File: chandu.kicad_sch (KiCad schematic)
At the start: 37 parts, among them IC1 bp060674p12, IC2 bp060674p12, J1 B5B-XH-A, J3 B5B-XH-A, J4 B2B-XH-A__LF__SN_, J5 B2B-XH-A__LF__SN_, J6 B4B-XH-A_LF__SN_, J7 51494-2, J8 51494-2, U1 KY-040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

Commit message: Initialtes
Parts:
- removed R_dac2_pup_scl1, R_dac2_pup_sda1, R_oled_pup_scl1, R_oled_pup_sda1: 4.7k, Resistor_THT:R_Axial_DIN0207_L6.3mm_D2.5mm_P7.62mm_Horizontal, symbol Device:R
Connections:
- net 3.3V: now also R_dac1_pup_scl1.2; no longer R_dac1_pup_scl1.1
- net at J6.2, U2.33 (IO21), U6.5 (SCL)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: now also R_dac1_pup_scl1.1; no longer R_dac1_pup_scl1.2
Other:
- moved on the sheet: D2, R_dac1_pup_scl1, R_dac1_pup_sda1

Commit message: Initialtes
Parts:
- U2: footprint kaam25_footprints_symbol:MODULE_DEVKIT_V1_ESP32-WROOM-32 -> kaam25:MODULE_DEVKIT_V1_ESP32-WROOM-32; Distributer https://robu.in/product/esp-wroom-32-wifi-bluetooth-network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 -> (none)
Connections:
- net 3.3V: no longer U2.1 (3V3)
- net GND2: now also U2.13 (IO12); no longer U2.14 (GND1)
- net at J6.3, R_dac1_pup_sda1.2, U6.4 (SDA)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: now also U2.37 (IO23); no longer U2.36 (IO22)
- net at J6.2, R_dac1_pup_scl1.1, U6.5 (SCL)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: now also U2.34 (RXD0); no longer U2.33 (IO21)
- net at R1.2, R3.1: now also U2.5 (IO34); no longer U2.6 (IO35)
- net at J5.1: now also U2.38 (GND3); no longer U2.37 (IO23)
- net at R5.2, R7.1: now also U2.7 (IO32); no longer U2.8 (IO33)
- net at R6.2, R8.1: now also U2.3 (SENSOR_VP); no longer U2.4 (SENSOR_VN)
- net at R2.2, R4.1: now also U2.2 (EN); no longer U2.3 (SENSOR_VP)
- net at U2.10 (IO26): now also J1.1; no longer J3.3
- net at U2.11 (IO27): no longer J1.1
- net at J3.5: now also U2.14 (GND1); no longer U2.15 (IO13)
- net at U2.26 (IO4): no longer J4.2
- net at U2.27 (IO16): now also J4.2
- net at U2.31 (IO19): no longer J3.4
- net at U2.32 (GND2): now also J3.4
- net at J1.3: now also U2.4 (SENSOR_VN); no longer U2.5 (IO34)
- net at J1.2: now also U2.6 (IO35); no longer U2.7 (IO32)
- net at U2.9 (IO25): now also J3.3
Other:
- moved on the sheet: J4

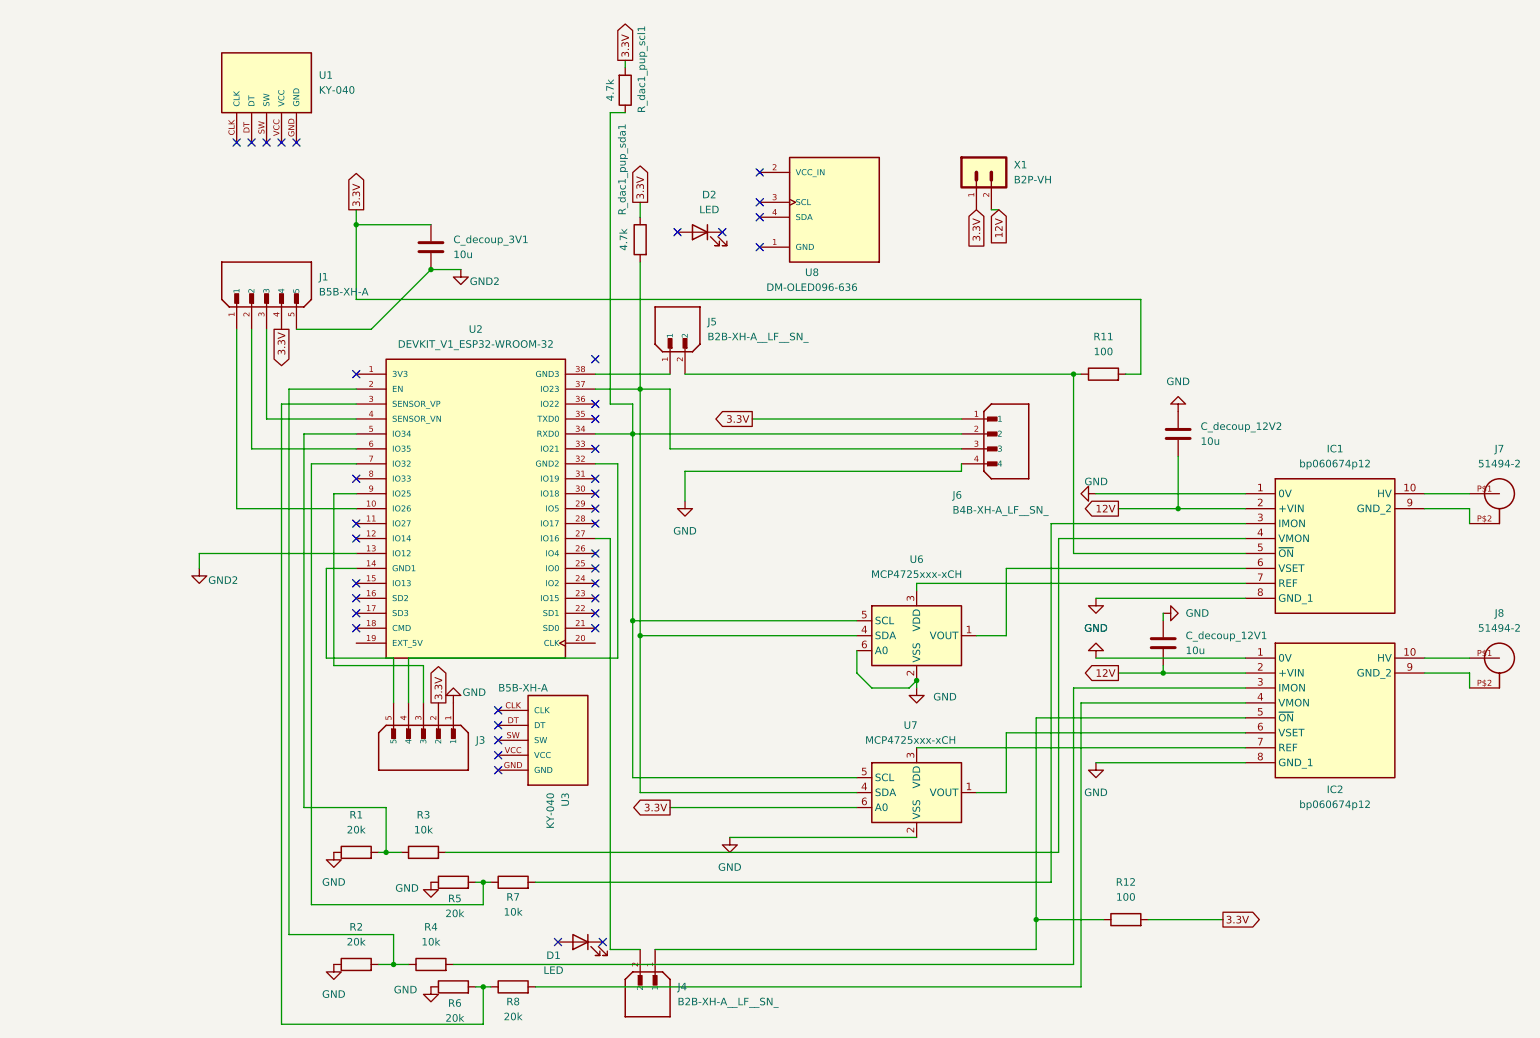
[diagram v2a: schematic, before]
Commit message: Initialtes gndplane
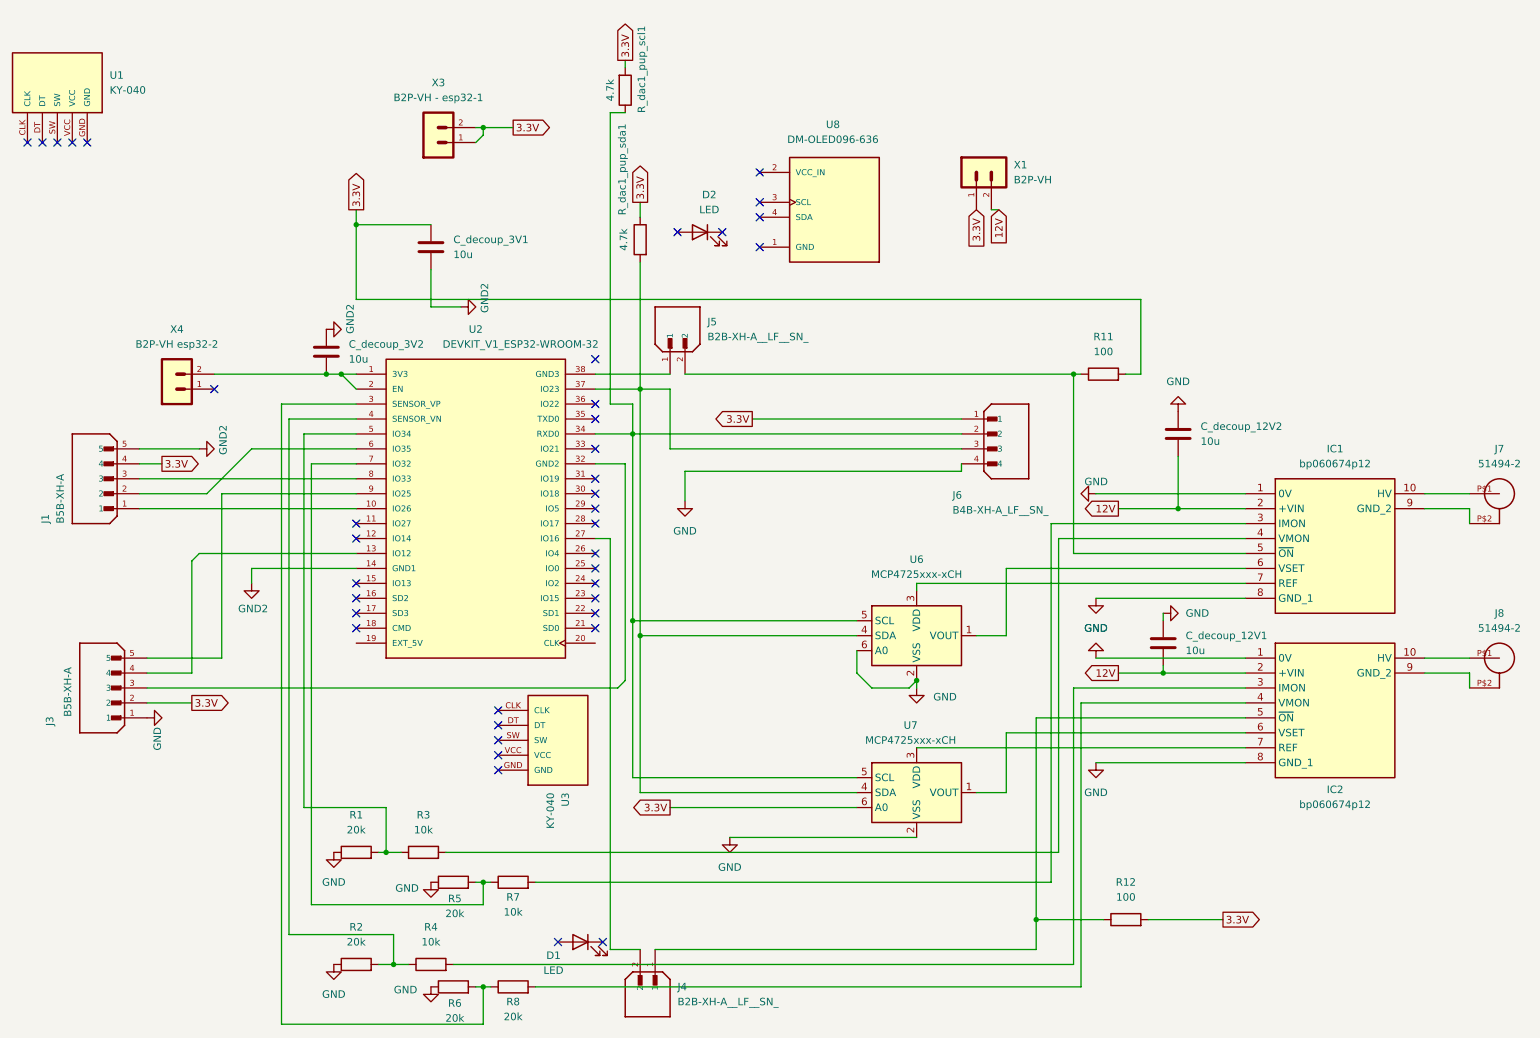
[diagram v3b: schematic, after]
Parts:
- added C_decoup_3V2: 10u, Capacitor_THT:CP_Radial_D5.0mm_P2.00mm, symbol Device:C
- added X3: B2P-VH - esp32-1, symbol B2P-VH:B2P-VH
- added X4: B2P-VH esp32-2, symbol B2P-VH:B2P-VH
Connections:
- net 3.3V: now also X3.1, X3.2
- net GND2: now also U2.14 (GND1), C_decoup_3V2.1; no longer U2.13 (IO12)
- net at R2.2, R4.1: now also U2.4 (SENSOR_VN); no longer U2.2 (EN)
- net at U2.1 (3V3): now also U2.2 (EN), C_decoup_3V2.2, X4.2
- net at J3.5: now also U2.9 (IO25); no longer U2.14 (GND1)
- net at J3.4: now also U2.13 (IO12); no longer U2.32 (GND2)
- net at J1.3: now also U2.8 (IO33); no longer U2.4 (SENSOR_VN)
- net at J3.3: now also U2.32 (GND2); no longer U2.9 (IO25)
- no-connect marks 40 -> 39
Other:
- moved on the sheet: J1, J3, U1

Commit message: Initialtes apr22
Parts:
- removed X3: B2P-VH - esp32-1, symbol B2P-VH:B2P-VH
- removed X4: B2P-VH esp32-2, symbol B2P-VH:B2P-VH
- added J10, J9: B2B-XH-A, kaam25:B2P-VH, symbol B2B-XH-A:B2B-XH-A
- J1, J3: value B5B-XH-A -> B5B-XH-A_rotataryKnob
- J4, J5: value B2B-XH-A__LF__SN_ -> B2B-XH-A__LF__SN_ledTwoTerminal
- J6: value B4B-XH-A_LF__SN_ -> B4B-XH-A_LF__SN_oled_display
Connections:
- net 3.3V: now also J10.1, J10.2
- net at C_decoup_3V2.2, U2.1 (3V3), U2.2 (EN): now also J9.2

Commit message: Initialtes apr24
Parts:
- added X3: B2P-VH, Connector_JST:JST_VH_B2P-VH-B_1x02_P3.96mm_Vertical, symbol B2P-VH:B2P-VH
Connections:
- net GND2 is gone; now on net GND1: C_decoup_3V1.2, C_decoup_3V2.1, J1.5, U2.14 (GND1)
- net 12V: now also X3.2
- net 3.3V: now also X3.1; no longer J1.4
- net vset_a: now reaches IC1.6 (VSET), U6.1 (VOUT)
- net ref_b: now reaches IC1.7 (REF), U6.3 (VDD)
- net ref_b: now also IC2.7 (REF), U7.3 (VDD)
- net sda_a: now reaches J6.3, R_dac1_pup_sda1.2, U2.37 (IO23), U6.4 (SDA), U7.4 (SDA)
- net scl_a: now reaches J6.2, R_dac1_pup_scl1.1, U2.34 (RXD0), U6.5 (SCL), U7.5 (SCL)
- net \ON_b: now reaches IC2.5 (~{ON}), J4.1, R12.1
- net vset_b: now reaches IC2.6 (VSET), U7.1 (VOUT)
- net adc_V_a: now reaches R1.2, R3.1, U2.5 (IO34)
- net at U2.38 (GND3): no longer J5.1
- net \ON_a: now reaches IC1.5 (~{ON}), J5.2, R11.1
- net adc_I_a: now reaches R5.2, R7.1, U2.7 (IO32)
- net adc_V_b: now reaches R6.2, R8.1, U2.3 (SENSOR_VP)
- net adc_I_b: now reaches R2.2, R4.1, U2.4 (SENSOR_VN)
- net at C_decoup_3V2.2, J9.2, U2.1 (3V3)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: now also J1.4
- net CLK_a: now reaches J1.1, U2.10 (IO26)
- net at U2.13 (IO12): no longer J3.4
- net led_b: now reaches J4.2, U2.27 (IO16)
- net CLK_b: now reaches U2.30 (IO18)
- net CLK_b: now also J3.5
- net DT_b: now reaches U2.31 (IO19)
- net DT_b: now also J3.4
- net SW_B: now reaches J3.3, U2.32 (GND2)
- net led_a: now reaches U2.33 (IO21)
- net led_a: now also J5.1
- net DT_a: now reaches J1.2, U2.6 (IO35)
- net SW_a: now reaches J1.3, U2.8 (IO33)
- net at U2.9 (IO25): no longer J3.5
- net GND renamed GND1
- no-connect marks 39 -> 38
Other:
- moved on the sheet: D1, J4

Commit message: Initialtes apr26
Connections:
- net ref_b: no longer IC1.7 (REF), U6.3 (VDD)
- net i_mon_b: now reaches IC2.3 (IMON), R4.2
- net v_mon_b: now reaches IC2.4 (VMON), R8.2
- net v_mon_a: now reaches IC1.4 (VMON), R3.2
- net i_mon_a: now reaches IC1.3 (IMON), R7.2
- new net ref_a: IC1.7 (REF), U6.3 (VDD)
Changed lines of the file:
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@@
 	)
 	(junction
-		(at 76.2 46.99)
-		(diameter 0)
-		(color 0 0 0 0)
-	)
-	(junction
 		(at 81.28 153.67)
 		(diameter 0)
@@
 	)
 	(junction
+		(at 76.2 46.99)
+		(diameter 0)
+		(color 0 0 0 0)
+	)
+	(junction
 		(at 55.88 72.39)
 		(diameter 0)
@@
 	(wire
 		(pts
+			(xy 44.45 130.81) (xy 40.64 130.81)
+		)
+		(stroke
+			(width 0)
+			(type default)
+		)
+	)
+	(wire
+		(pts
 			(xy 40.64 120.65) (xy 118.11 120.65)
 		)
@@
 		)
 	)
+	(label "i_mon_b"
+		(at 214.63 125.73 0)
+		(effects
+			(font
+				(size 1.27 1.27)
+			)
+			(justify left bottom)
+		)
+	)
+	(label "v_mon_b"
+		(at 214.63 128.27 0)
+		(effects
+			(font
+				(size 1.27 1.27)
+			)
+			(justify left bottom)
+		)
+	)
 	(label "scl_a"
 		(at 135.89 114.3 0)
@@
 		)
 	)
-	(label "ref_b"
+	(label "ref_a"
 		(at 218.44 107.95 0)
 		(effects
@@
 		)
 	)
+	(label "v_mon_a"
+		(at 215.9 100.33 0)
+		(effects
+			(font
+				(size 1.27 1.27)
+			)
+			(justify left bottom)
+		)
+	)
 	(label "adc_I_a"
 		(at 69.85 87.63 0)
@@
 		)
 	)
+	(label "i_mon_a"
+		(at 215.9 97.79 0)
+		(effects
+			(font
+				(size 1.27 1.27)
+			)
+			(justify left bottom)
+		)
+	)
 	(label "DT_b"
 		(at 43.18 123.19 0)
@@
 	(symbol
 		(lib_id "power:GND1")
-		(at 40.64 130.81 90)
+		(at 44.45 130.81 90)
 		(unit 1)
 		(body_style 1)
@@
 		(fields_autoplaced yes)
 		(property "Reference" "#PWR052"
-			(at 46.99 130.81 0)
+			(at 50.8 130.81 0)
 			(hide yes)
 			(show_name no)
@@
 		)
 		(property "Value" "GND1"
-			(at 44.45 130.8099 90)
+			(at 48.26 130.8099 90)
 			(show_name no)
 			(do_not_autoplace no)
@@
 		)
 		(property "Footprint" ""
-			(at 40.64 130.81 0)
+			(at 44.45 130.81 0)
 			(hide yes)
 			(show_name no)
@@
 		)
 		(property "Datasheet" ""
-			(at 40.64 130.81 0)
+			(at 44.45 130.81 0)
 			(hide yes)
 			(show_name no)
@@
 		)
 		(property "Description" "Power symbol creates a global label with name \"GND1\" , ground"
-			(at 40.64 130.81 0)
+			(at 44.45 130.81 0)
 			(hide yes)
 			(show_name no)

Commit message: Initialtes draft1
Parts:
- removed C_decoup_3V1: 10u, Capacitor_THT:CP_Radial_D5.0mm_P2.00mm, symbol Device:C
- removed J10, J9: B2B-XH-A, kaam25:B2P-VH, symbol B2B-XH-A:B2B-XH-A
- removed X1: B2P-VH, Connector_JST:JST_VH_B2P-VH-B_1x02_P3.96mm_Vertical, symbol B2P-VH:B2P-VH
- added X4, X5: B2P-VH, Connector_JST:JST_VH_B2P-VH-B_1x02_P3.96mm_Vertical, symbol B2P-VH:B2P-VH
- C_decoup_12V1, C_decoup_12V2: KiLib_Generator (none) -> capacitor/THT/other
- C_decoup_3V3_2: renamed from C_decoup_3V2; KiLib_Generator (none) -> capacitor/THT/other
- D1, D2: KiLib_Generator (none) -> LED/THT
- R1, R11, R12, R2, R3, R4, R5, R6, R7, R8, R_dac1_pup_scl1, R_dac1_pup_sda1: KiLib_Generator (none) -> resistor/THT
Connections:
- net 12V: now also X3.1, X5.1; no longer X3.2
- net 3.3V: now also X3.2, X5.2; no longer J3.2, J6.1, R11.2, R12.2, R_dac1_pup_scl1.2, R_dac1_pup_sda1.1, X3.1
- net 3v3_esp32: now reaches C_decoup_3V3_2.2, J1.4, U2.1 (3V3), U2.2 (EN)
- net 3v3_esp32: now also J3.2, J6.1, R11.2, R12.2, R_dac1_pup_scl1.2, R_dac1_pup_sda1.1, X4.2
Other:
- note added: "i2c pull ups is by esp32"
- note added: "voltsgr for esp32 & bps vcc _ 1"
- note added: "voltsgr for esp32 & bps vcc _2"
